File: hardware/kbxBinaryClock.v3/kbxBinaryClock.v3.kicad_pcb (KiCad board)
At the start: 2 copper layers, 127 x 114.3 mm, 136 parts, among them J1 Jack-DC, J2 Conn_01x06, J3 Conn_02x03_Odd_Even, P1 STM32_SWD_USART, Q1 2N7002, Q10 Q_NPN_BCE, Q11 Q_NPN_BCE, Q2 2N7002, Q3 2N7002, Q4 2N7002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

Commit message: Updated Silkscreen for volume mode and added clearer pin 1 markings for ICs
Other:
- board text added: "."
- board text added: "RESET SUPERVISOR"
- board text added: "RGB Binary Clock version 3.0.3 Designed by Keith Burzinski (@kbx81) in Chicago, Illinois Source & other details: https://github.com/kbx81/RGBBinaryClock Layout inspired by EKI, Inc. kit 798"
- board text removed: "RGB Binary Clock version 3.0.2 Designed by Keith Burzinski (@kbx81) in Chicago, Illinois Source & other details: https://github.com/kbx81/RGBBinaryClock Layout inspired by EKI, Inc. kit 798"
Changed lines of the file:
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@@
     (area 92.151429 32.944999 222.808572 147.514525)
     (thickness 1.6)
-    (drawings 33)
+    (drawings 42)
     (tracks 2967)
     (zones 0)
@@
     (34 B.Paste user)
     (35 F.Paste user)
-    (36 B.SilkS user hide)
+    (36 B.SilkS user)
     (37 F.SilkS user)
     (38 B.Mask user)
@@
       (net 155 "Net-(SB2-Pad2)"))
   )
+  (gr_text . (at 200.787 89.789) (layer F.SilkS)
+    (effects (font (size 2 2) (thickness 0.5)))
+  )
+  (gr_text . (at 177.419 123.19) (layer F.SilkS)
+    (effects (font (size 2 2) (thickness 0.5)))
+  )
+  (gr_text . (at 177.419 115.316) (layer F.SilkS)
+    (effects (font (size 2 2) (thickness 0.5)))
+  )
+  (gr_text . (at 163.449 115.443) (layer F.SilkS)
+    (effects (font (size 2 2) (thickness 0.5)))
+  )
+  (gr_text . (at 144.272 114.3) (layer F.SilkS)
+    (effects (font (size 2 2) (thickness 0.5)))
+  )
+  (gr_text . (at 177.546 103.632) (layer F.SilkS)
+    (effects (font (size 2 2) (thickness 0.5)))
+  )
+  (gr_text . (at 147.066 103.632) (layer F.SilkS)
+    (effects (font (size 2 2) (thickness 0.5)))
+  )
+  (gr_text . (at 116.586 103.632) (layer F.SilkS)
+    (effects (font (size 2 2) (thickness 0.5)))
+  )
+  (gr_text "RESET\nSUPERVISOR" (at 167.64 116.84 90) (layer B.SilkS)
+    (effects (font (size 0.75 0.75) (thickness 0.15)) (justify mirror))
+  )
   (gr_text "9 to 12 Volts DC\n2 Amps\nPositive (+) Tip" (at 217.17 135.382) (layer B.SilkS)
     (effects (font (size 0.75 0.75) (thickness 0.15)) (justify left mirror))
@@
     (effects (font (size 0.75 0.75) (thickness 0.15)) (justify left mirror))
   )
-  (gr_text "Modes:\n====\n1: Fixed Display\n2: Toggle Display\n3: Timer/Counter\n5: Set Time\n6: Set Date\n10: Set System Options/Config Bits\n11: Set Slot Beep Enable Bits\n12: Set Slot Blink Enable Bits\n13: Set Slot Color Change Enable Bits\n20: Set Duration of Time Display Value (in Toggle Mode 2)\n21: Set Duration of Date Display Value (in Toggle Mode 2)\n22: Set Duration of Temperature Display Value (in Toggle Mode 2)\n23: Set Duration of Fade as Bits Change Value\n24: Set DST Begin Month Value\n25: Set DST Begin Day of Week Ordinal Value\n26: Set DST End Month Value\n27: Set DST End Day of Week Ordinal Value\n28: Set DST Switch Day of Week Value\n29: Set DST Switch Hour Value\n30: Set Minimum Display Intensity Value\n31: Set Flicker Reduction Threshold Value\n32: Set Current Drive Level Value\n33: Set Temperature Calibration Value\n34: Set DMX-512 Address Value\n40 - 47: Set Slot 1 through 8 Time\n50 - 57: Set Slot 1 through 8 Colors\n58: Set Date Colors\n59: Set Temperature Colors\n60: Set Timer/Counter Colors" (at 207.518 101.981) (layer B.SilkS)
+  (gr_text "Modes:\n====\n1: Fixed Display\n2: Toggle Display\n3: Timer/Counter\n5: Set Time\n6: Set Date\n10: Set System Options/Config Bits\n11: Set Slot Beep Enable Bits\n12: Set Slot Blink Enable Bits\n13: Set Slot Color Change Enable Bits\n20: Set Duration of Time Display Value (in Toggle Mode 2)\n21: Set Duration of Date Display Value (in Toggle Mode 2)\n22: Set Duration of Temperature Display Value (in Toggle Mode 2)\n23: Set Duration of Fade as Bits Change Value\n24: Set DST Begin Month Value\n25: Set DST Begin Day of Week Ordinal Value\n26: Set DST End Month Value\n27: Set DST End Day of Week Ordinal Value\n28: Set DST Switch Day of Week Value\n29: Set DST Switch Hour Value\n30: Set Minimum Display Intensity Value\n31: Set Flicker Reduction Threshold Value\n32: Set Current Drive Level Value\n33: Set Temperature Calibration Value\n34: Set Beeper (Alarm) Volume\n39: Set DMX-512 Address Value\n40 - 47: Set Slot 1 through 8 Time\n50 - 57: Set Slot 1 through 8 Colors\n58: Set Date Colors\n59: Set Temperature Colors\n60: Set Timer/Counter Colors" (at 207.518 101.981) (layer B.SilkS)
     (effects (font (size 0.75 0.75) (thickness 0.15)) (justify left mirror))
   )
@@
     (effects (font (size 1 1) (thickness 0.2)))
   )
-  (gr_text "RGB Binary Clock version 3.0.2\nDesigned by Keith Burzinski (@kbx81) in Chicago, Illinois\nSource & other details: https://github.com/kbx81/RGBBinaryClock\nLayout inspired by EKI, Inc. kit 798" (at 105.41 39.37) (layer F.SilkS)
+  (gr_text "RGB Binary Clock version 3.0.3\nDesigned by Keith Burzinski (@kbx81) in Chicago, Illinois\nSource & other details: https://github.com/kbx81/RGBBinaryClock\nLayout inspired by EKI, Inc. kit 798" (at 105.41 39.37) (layer F.SilkS)
     (effects (font (size 0.75 0.75) (thickness 0.15)) (justify left))
   )

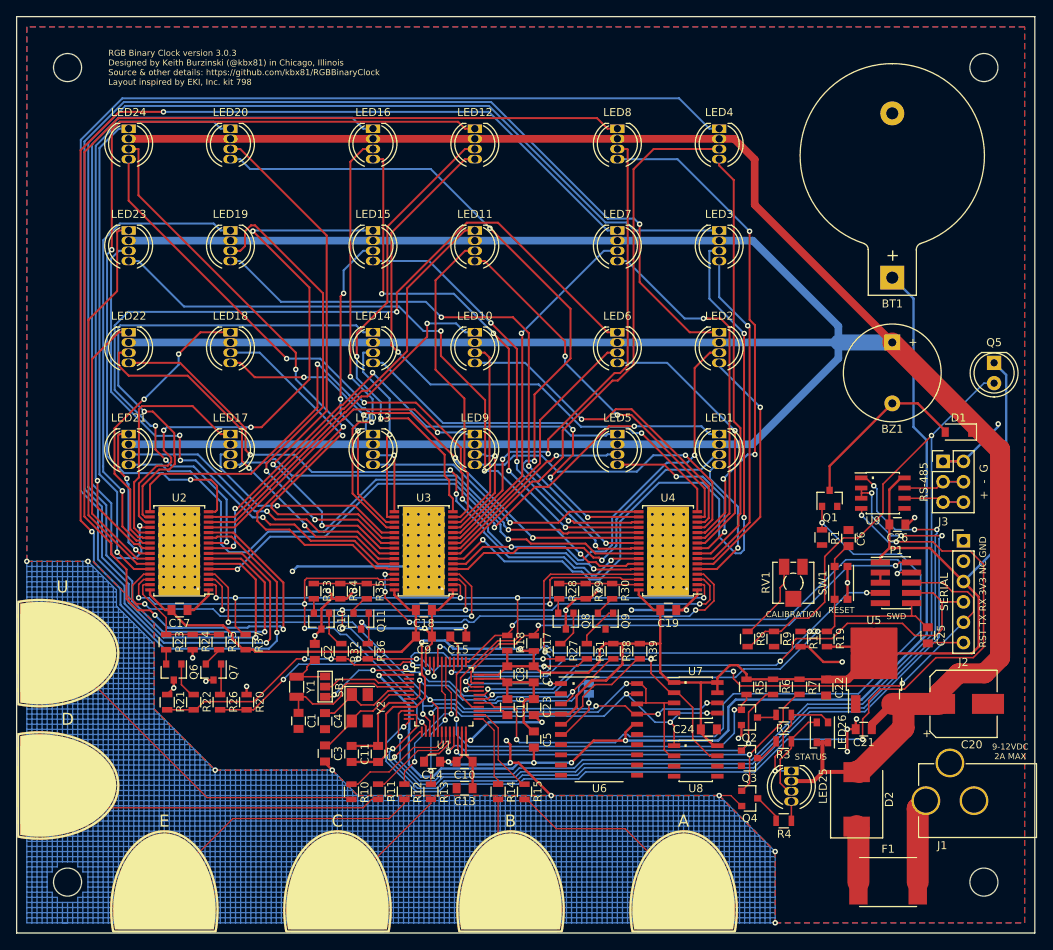
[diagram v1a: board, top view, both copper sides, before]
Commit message: Updated slikscreen, minor tweaks
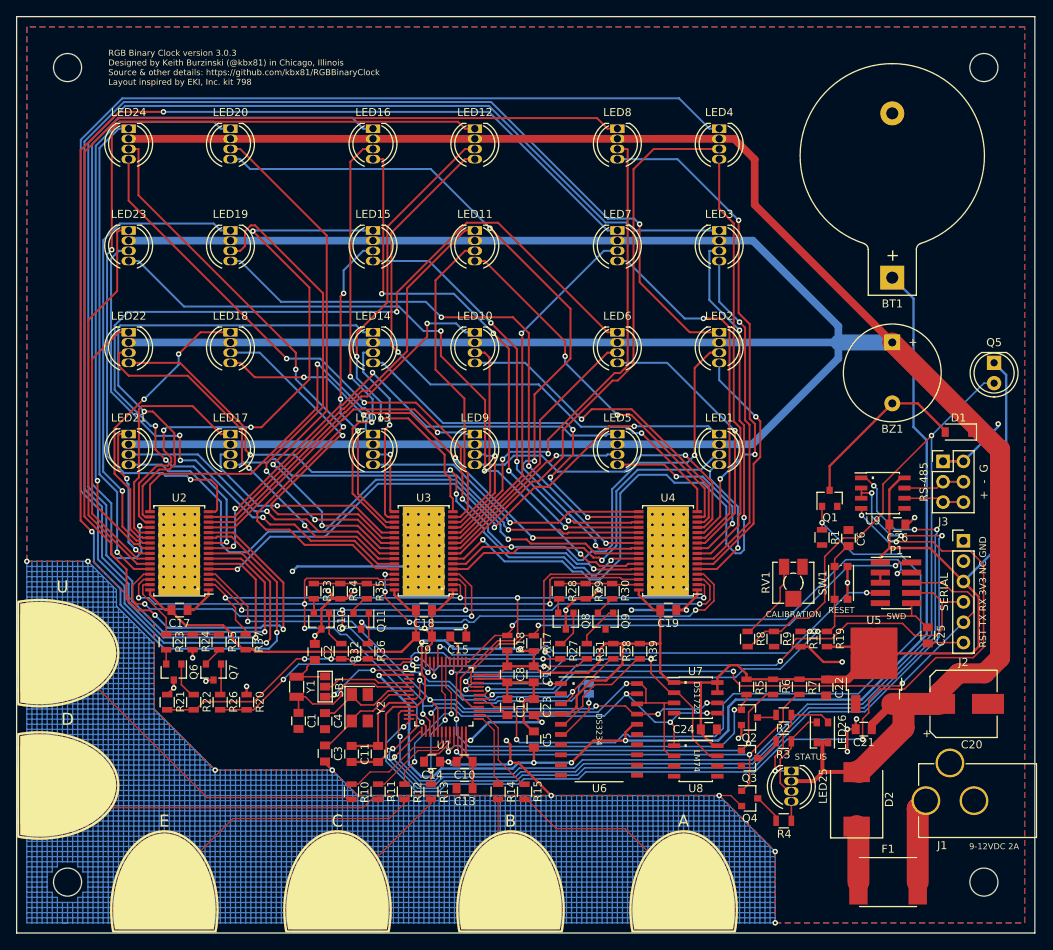
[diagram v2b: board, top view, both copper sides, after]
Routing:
- net LED3_G: track 94.0 -> 96.9 mm
- net LED2_G: track 53.9 -> 55.9 mm
- net LED1_G: track 42.4 -> 44.4 mm
- net /Display/SPI1_MOSI: track 78.5 -> 77.0 mm
- net /Display/SPI1_SCK: track 139.1 -> 137.7 mm
- net LED5_B: track 23.5 -> 24.3 mm
- net /Display/BLANK: track 92.8 -> 92.5 mm, vias 5 -> 4
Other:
- board text added: "9-12VDC 2A"
- board text added: "DS1722"
- board text added: "DS3234"
- board text added: "LM74"
- board text removed: "9-12VDC 2A MAX"

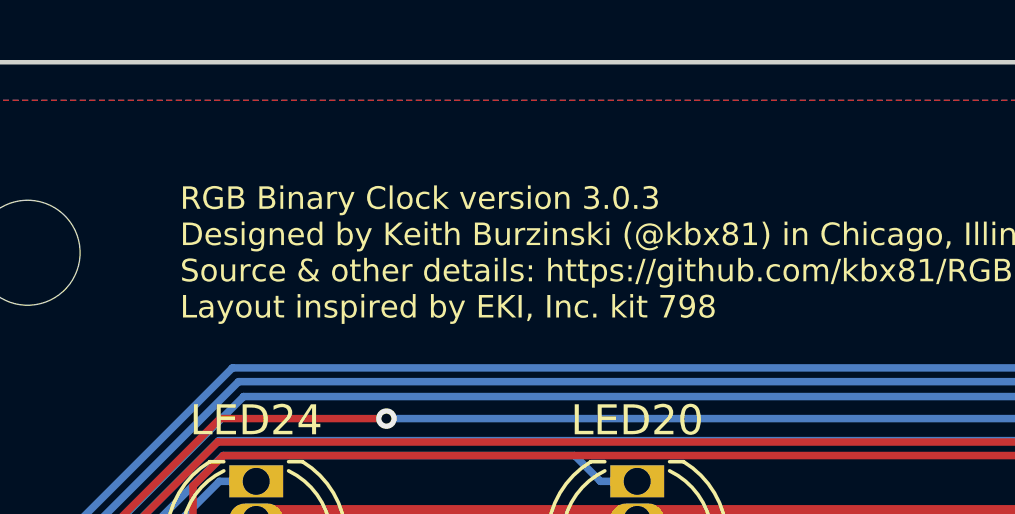
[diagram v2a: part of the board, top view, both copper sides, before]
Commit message: Updated for KiCad v5, updated silks
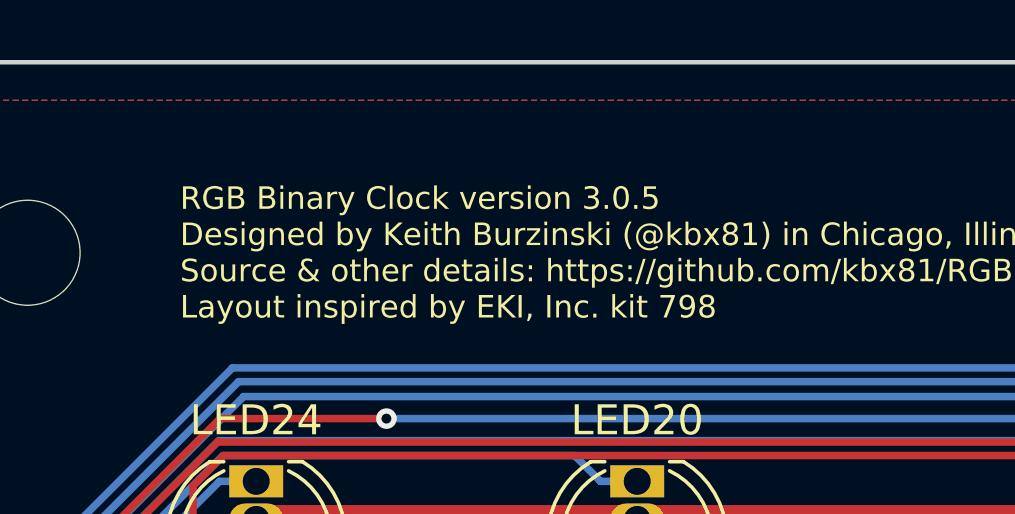
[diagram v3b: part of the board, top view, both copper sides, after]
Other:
- board text added: "DEFAULT TO TOGGLE"
- board text added: "MSbs OFF"
- board text added: "Modes: ==== 1: Fixed Display 2: Toggle Display 3: Timer/Counter 4: DMX-512 Display 5: Set Time 6: Set Date 7: Set Timer Reset Value 10: Set System Options/Config Bits 11: Set Slot Beep Enable Bits 12: Set Slot Blink Enable Bits 13: Set Slot Color Change Enable Bits 20: Set Duration of Time Display Value (in Toggle Mode 2) 21: Set Duration of Date Display Value (in Toggle Mode 2) 22: Set Duration 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"
- board text added: "RGB Binary Clock version 3.0.5 Designed by Keith Burzinski (@kbx81) in Chicago, Illinois Source & other details: https://github.com/kbx81/RGBBinaryClock Layout inspired by EKI, Inc. kit 798"
- board text removed: "Modes: ==== 1: Fixed Display 2: Toggle Display 3: Timer/Counter 5: Set Time 6: Set Date 10: Set System Options/Config Bits 11: Set Slot Beep Enable Bits 12: Set Slot Blink Enable Bits 13: Set Slot Color Change Enable Bits 20: Set Duration of Time Display Value (in Toggle Mode 2) 21: Set Duration of Date Display Value (in Toggle Mode 2) 22: Set Duration of Temperature Display Value (in Toggle Mode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"
- board text removed: "RGB Binary Clock version 3.0.3 Designed by Keith Burzinski (@kbx81) in Chicago, Illinois Source & other details: https://github.com/kbx81/RGBBinaryClock Layout inspired by EKI, Inc. kit 798"
